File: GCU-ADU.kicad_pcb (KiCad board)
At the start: 2 copper layers, 48.6 x 32.4 mm, 5 parts, among them X1 SW_Push, Y1 SW_Push

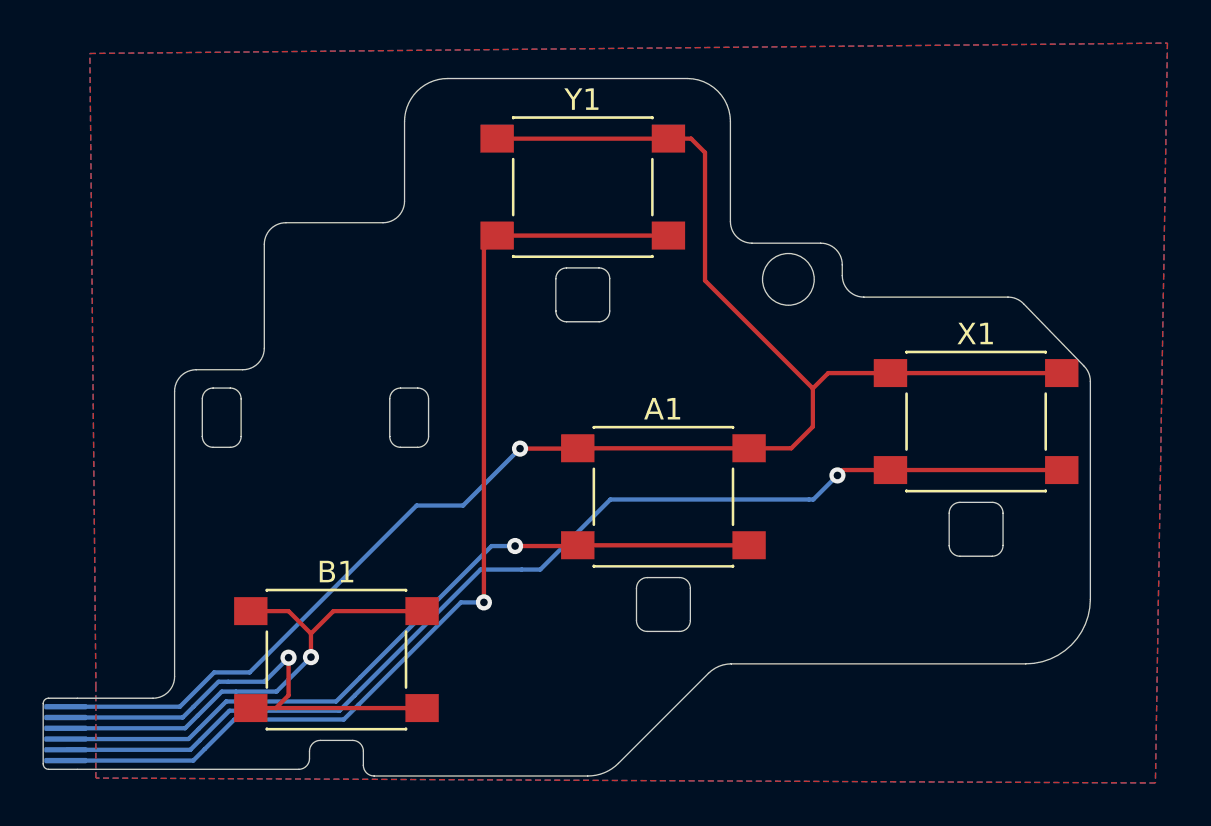
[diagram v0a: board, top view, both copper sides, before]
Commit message: Resolve backwards connector pins
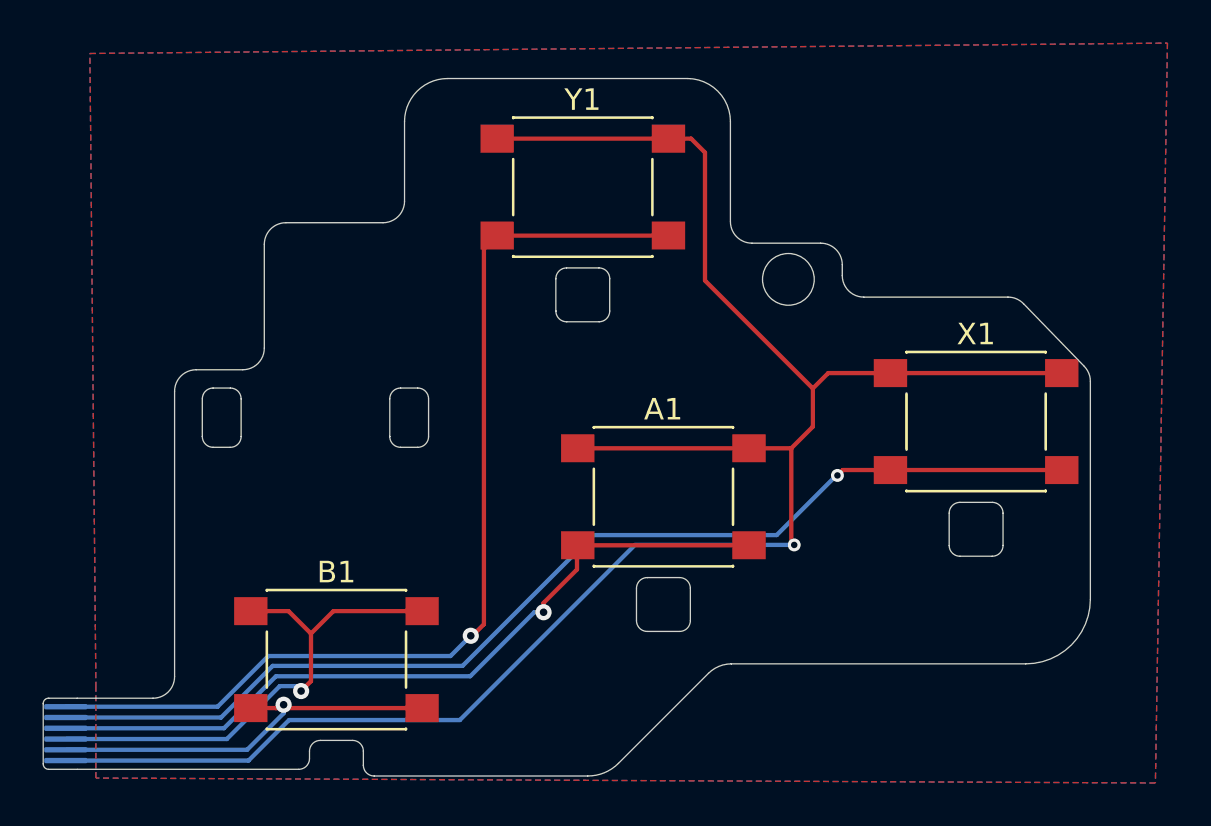
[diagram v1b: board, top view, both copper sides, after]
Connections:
- PINS1 pad 1: X1 -> X4
- PINS1 pad 2: X5 -> X3
- PINS1 pad 3: X6 -> X2
- PINS1 pad 4: X2 -> X6
- PINS1 pad 5: X3 -> X5
- PINS1 pad 6: X4 -> X1
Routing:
- net X1: track 76.6 -> 90.4 mm
- net X5: track 22.0 -> 19.6 mm
- net X6: track 22.7 -> 23.7 mm
- net X2: track 35.4 -> 36.1 mm
- net X3: track 51.6 -> 51.0 mm
